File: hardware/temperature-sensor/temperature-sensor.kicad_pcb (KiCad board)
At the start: 2 copper layers, 56 x 56 mm, 126 parts, among them IC1 SHT40-CD1B-R3, IC2 MAX5969BETB+T, IC3 LV2862XLVDDCR, IC4 LV2862XLVDDCR, J1 1149611, J2 219320-0001, J3 1990012, J4 ARM-JTAG-SWD, Q1 DMN3404L, Q2 DMN3404L, Q3 DMN3404L, Q4 DMN3404L, T1 SM13126PEL, U1 STM32F407V_E-G_Tx, U2 LAN8720A, U3 FT230XS, U4 AT24C512C, Y1 CX2016FB25000C0FZZH1

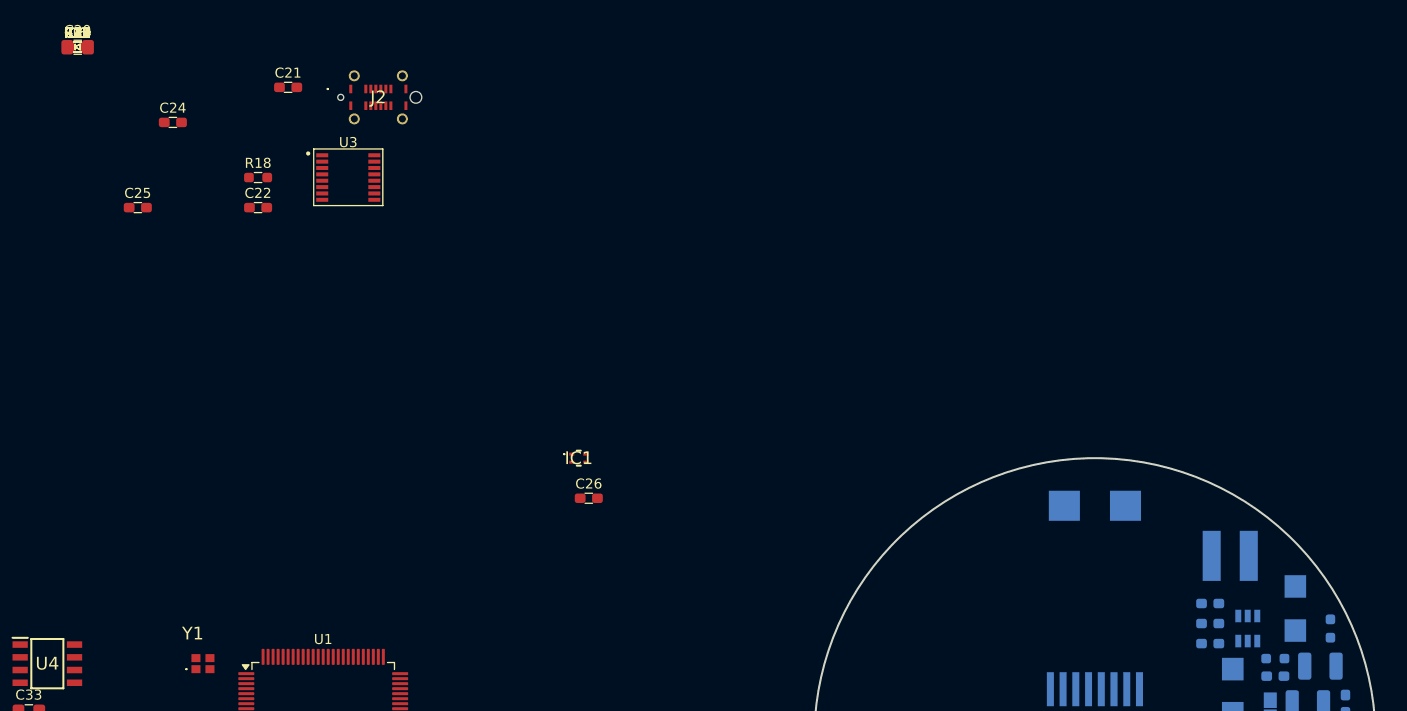
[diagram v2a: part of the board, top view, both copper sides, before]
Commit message: place USB footprints
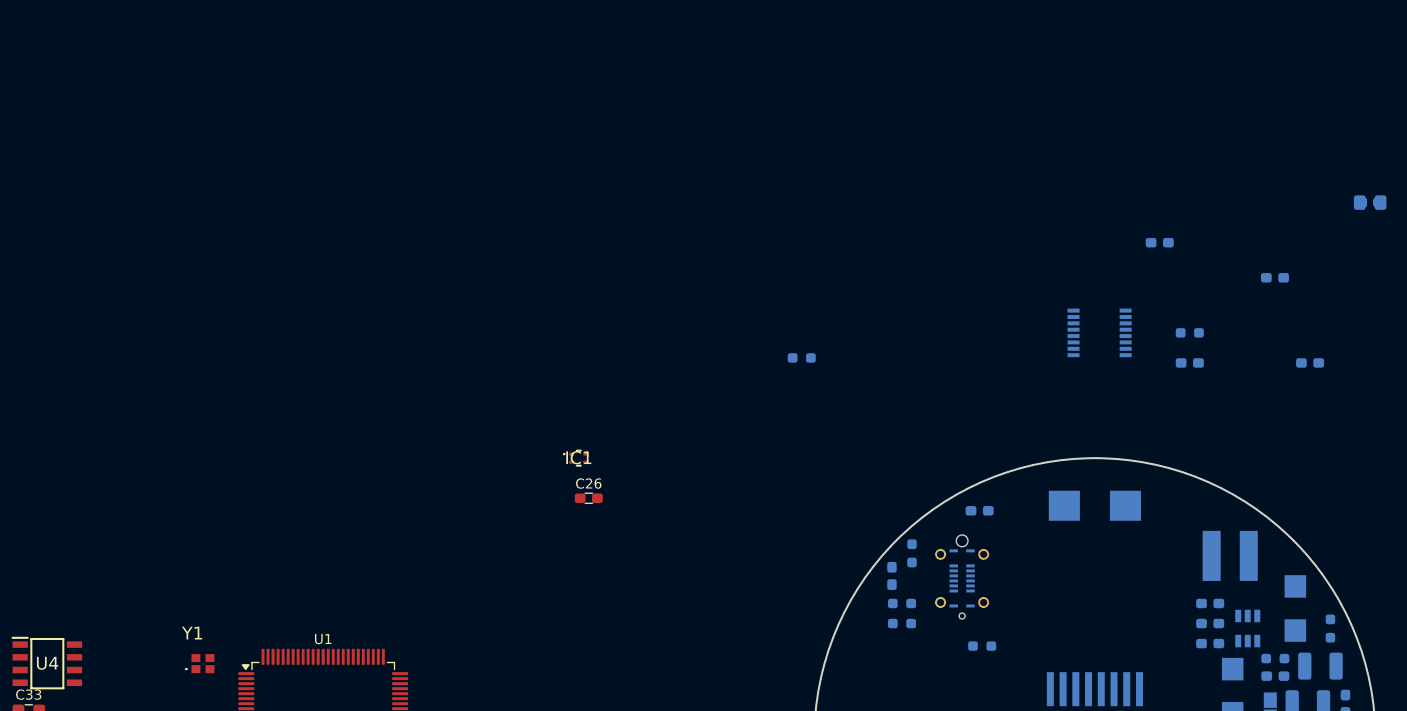
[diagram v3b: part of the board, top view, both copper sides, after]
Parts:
- C19, C20, C21, C22, C23, C24, C25, C32, D5, D6, FB2, J2, R14, R15, R18, R19, R20, R21, R22, R23, R28, R29, U3: moved to B.Cu
- moved C20 129.9 mm to (177.5, 45.5), turned to 180 degrees
- moved C23 129.9 mm to (177.5, 45.5), turned to 180 degrees
- moved D5 129.9 mm to (177.5, 45.5), turned to 180 degrees
- moved D6 129.9 mm to (177.5, 45.5), turned to 180 degrees
- moved R19 129.9 mm to (177.5, 45.5), turned to 180 degrees
- moved R20 129.9 mm to (177.5, 45.5), turned to 180 degrees
- moved R21 129.9 mm to (177.5, 45.5), turned to 180 degrees
- moved R22 129.9 mm to (177.5, 45.5), turned to 180 degrees
- moved R23 129.9 mm to (177.5, 45.5), turned to 180 degrees
- moved C25 118.0 mm to (171.5, 61.5), turned to 180 degrees
- moved C24 111.1 mm to (168.0, 53.0), turned to 180 degrees
- moved R29 108.2 mm to (138.8, 89.8)
- moved C32 101.2 mm to (138.5, 76.2), turned to 180 degrees
- moved R15 100.4 mm to (130.8, 87.5)
- moved R14 99.2 mm to (130.8, 85.5), turned to 180 degrees
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
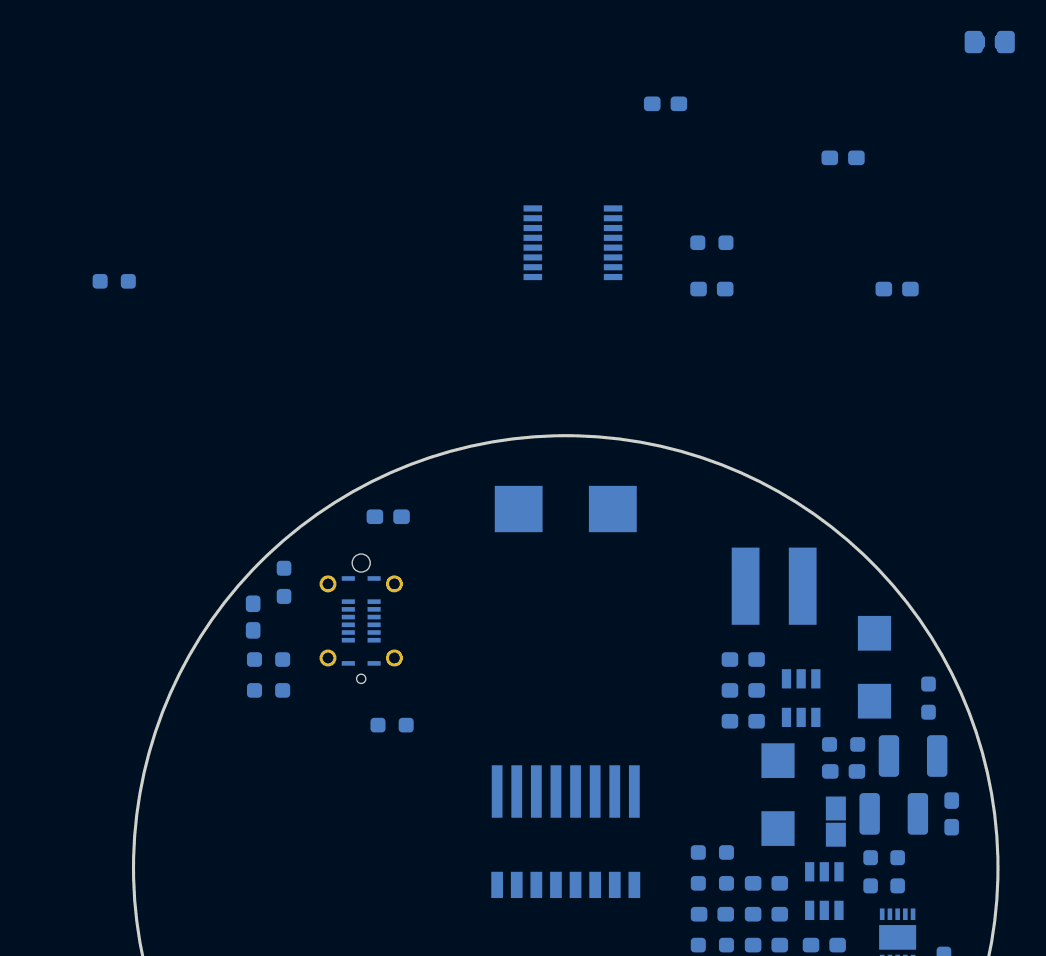
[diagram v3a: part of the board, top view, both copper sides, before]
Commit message: place USB footprints
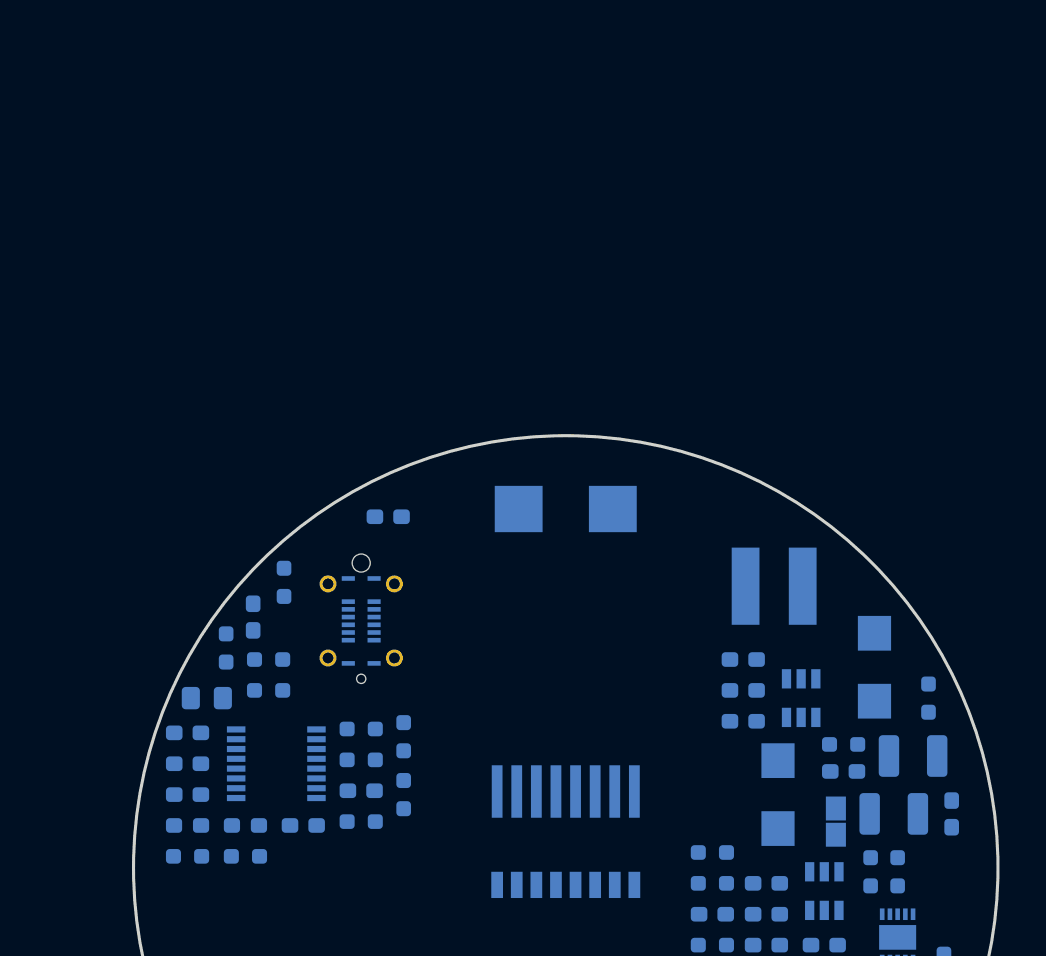
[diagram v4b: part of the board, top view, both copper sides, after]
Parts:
- moved D5 72.6 mm to (125.5, 96.2), turned to 0 degrees
- moved R19 71.5 mm to (129.2, 98.2)
- moved C23 71.3 mm to (125.5, 94.2)
- moved D6 70.0 mm to (129.2, 96.2)
- moved C20 66.2 mm to (126.8, 88.0)
- moved R21 64.9 mm to (136.8, 96.0)
- moved R22 61.8 mm to (136.8, 92.0)
- moved R23 61.8 mm to (139.5, 94.2), turned to -90 degrees
- moved R20 60.3 mm to (136.8, 90.0)
- moved C24 55.6 mm to (133.0, 96.2)
- moved R18 52.3 mm to (125.5, 98.2), turned to 0 degrees
- moved C21 51.2 mm to (125.5, 90.2)
- moved C25 47.6 mm to (136.8, 94.0), turned to 0 degrees
- moved C22 45.8 mm to (125.5, 92.2)
- moved U3 38.8 mm to (131.2, 92.2)
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
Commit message: place temperature sensor footprint
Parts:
- D8, Q1, R26, R27: moved to B.Cu
- moved R27 87.3 mm to (135.5, 101.0), turned to 180 degrees
- moved D8 81.5 mm to (130.5, 104.0), turned to 90 degrees
- moved U1 78.7 mm to (150.5, 112.2)
- moved Q1 77.9 mm to (135.0, 104.0), turned to 180 degrees
- moved R26 77.4 mm to (127.0, 106.2), turned to 180 degrees
- moved J3 72.3 mm to (131.0, 104.0), turned to 90 degrees
- moved C26 57.3 mm to (152.2, 97.5), turned to 90 degrees
- moved IC1 57.3 mm to (149.2, 97.5)

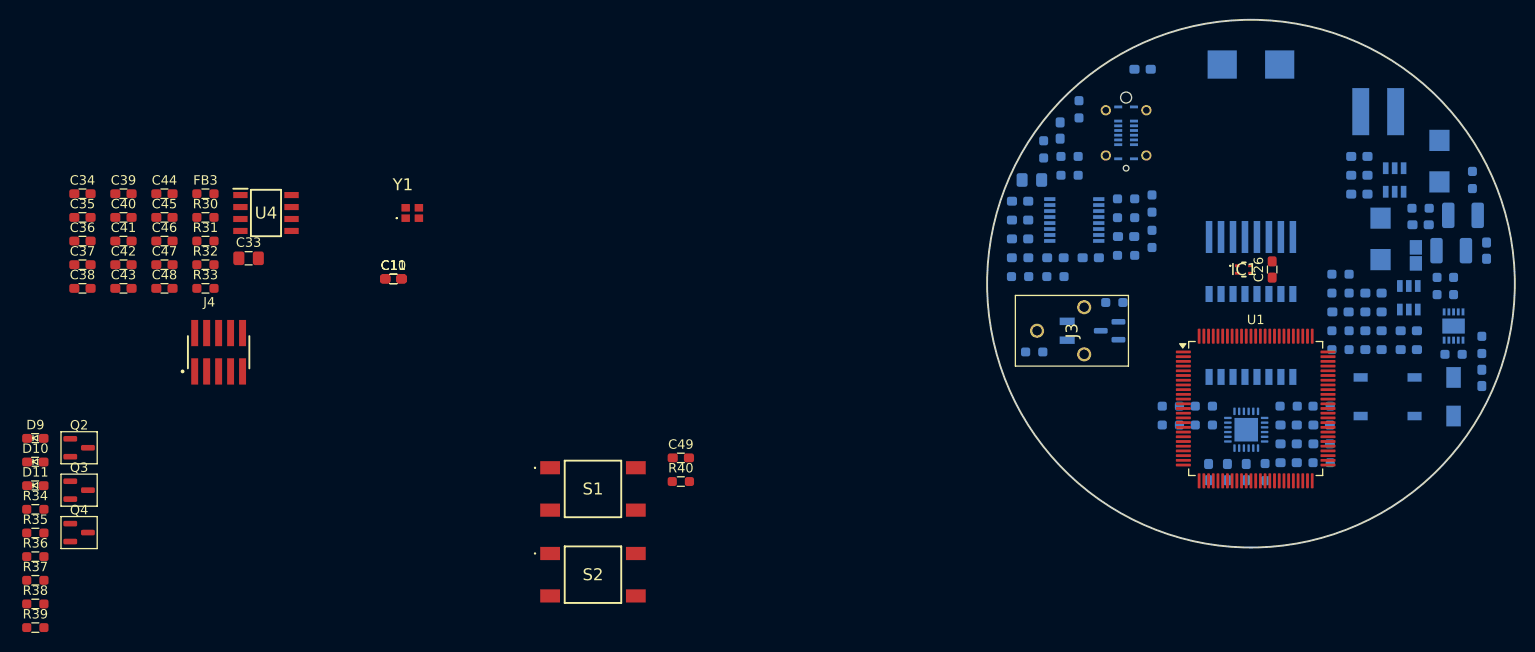
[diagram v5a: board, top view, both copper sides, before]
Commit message: finish placement
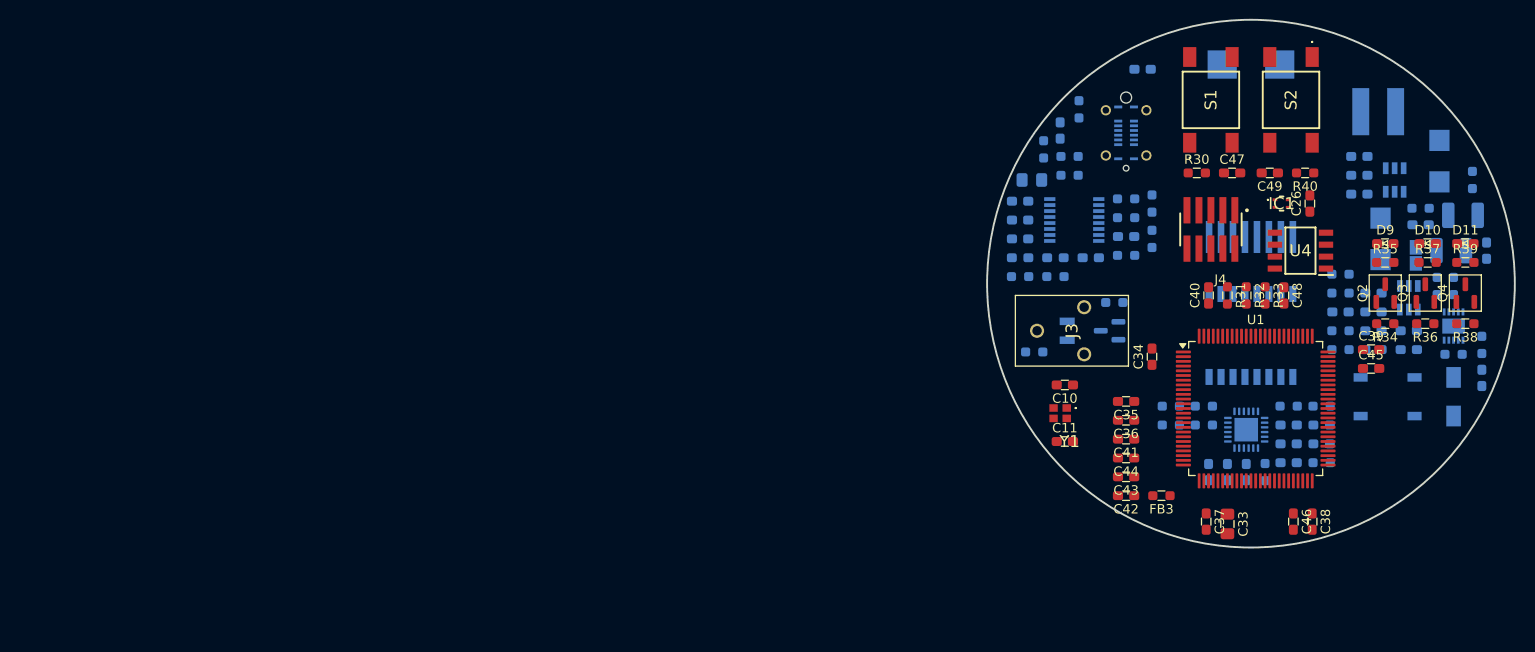
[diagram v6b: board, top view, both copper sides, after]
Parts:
- moved R39 156.6 mm to (172.8, 96.8)
- moved R38 154.6 mm to (172.8, 103.2), turned to 180 degrees
- moved D11 153.9 mm to (172.8, 94.8)
- moved R37 151.6 mm to (168.8, 96.8)
- moved D10 149.6 mm to (168.8, 94.8)
- moved R36 149.6 mm to (168.5, 103.2), turned to 180 degrees
- moved Q4 149.3 mm to (172.8, 100.0), turned to 90 degrees
- moved R35 146.1 mm to (164.2, 96.8)
- moved D9 144.7 mm to (164.2, 94.8)
- moved R34 144.6 mm to (164.2, 103.2), turned to 180 degrees
- moved Q3 144.4 mm to (168.5, 100.0), turned to 90 degrees
- moved Q2 139.6 mm to (164.2, 100.0), turned to 90 degrees
- moved C39 133.4 mm to (162.8, 106.0)
- moved C38 132.8 mm to (156.5, 124.2), turned to -90 degrees
- moved C45 129.0 mm to (162.8, 108.0)
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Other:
- board text added: "TEMP-SENSOR R01"
